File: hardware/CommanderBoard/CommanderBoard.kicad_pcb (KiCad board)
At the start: 2 copper layers, 63.5 x 106.7 mm, 42 parts, among them J1 Conn_01x22, J1BUS1 Conn_02x04_Odd_Even, J1BUS2 Conn_02x04_Odd_Even, J2 Conn_01x22, J2BUS1 Conn_01x02, J2BUS2 Conn_01x02, J3 HUB75, J4 Conn_01x22, SW1 SW_SPDT, SW2 SW_DP3T, SW3 SW_DP3T, SW4 SW_DP3T

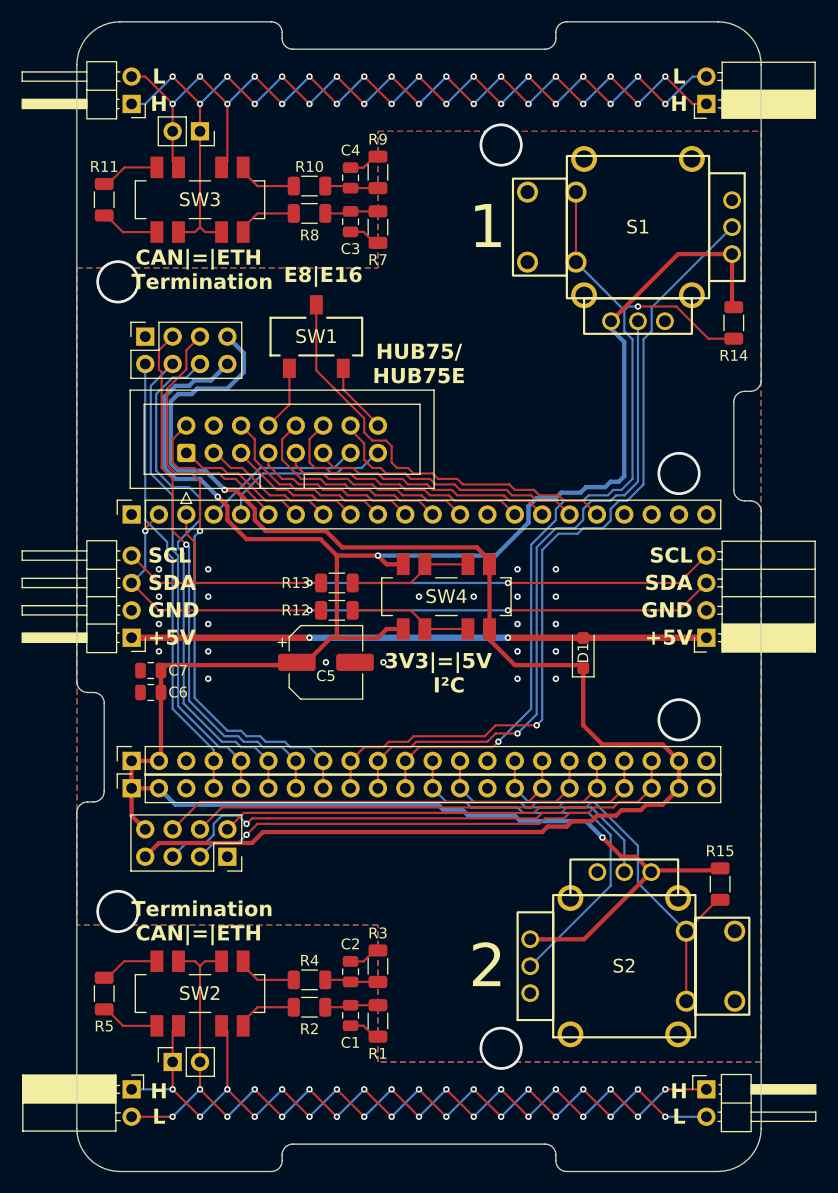
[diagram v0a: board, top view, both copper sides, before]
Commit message: Minor imrpovements in positions and footprints.
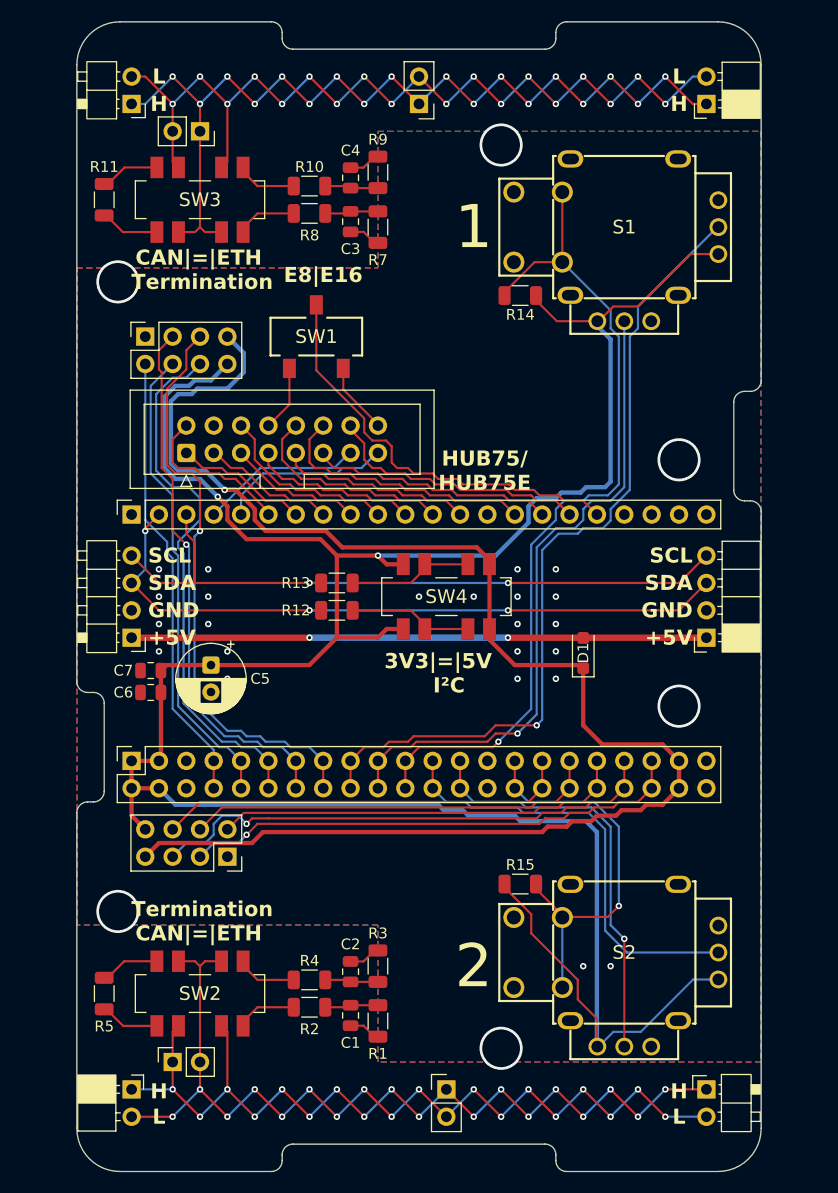
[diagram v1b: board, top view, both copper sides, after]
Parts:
- removed J4: Conn_01x22, Connector_PinSocket_2.54mm:PinSocket_1x22_P2.54mm_Vertical
- added BUS_TAP1: Conn_01x02_Socket, Connector_PinHeader_2.54mm:PinHeader_1x02_P2.54mm_Vertical, F.Cu at (129.5, 121.9)
- added BUS_TAP2: Conn_01x02_Socket, Connector_PinHeader_2.54mm:PinHeader_1x02_P2.54mm_Vertical, F.Cu at (127.0, 30.5)
- C5: footprint Capacitor_SMD:CP_Elec_6.3x7.7 -> Capacitor_THT:CP_Radial_D6.3mm_P2.50mm
- J2: value Conn_01x22 -> Conn_02x22; footprint Connector_PinSocket_2.54mm:PinSocket_1x22_P2.54mm_Vertical -> Connector_PinSocket_2.54mm:PinSocket_2x22_P2.54mm_Vertical
- moved R14 20.0 mm to (136.4, 48.3), turned to 180 degrees
- moved R15 18.5 mm to (136.4, 102.9), turned to 0 degrees
- moved C5 10.7 mm to (107.7, 82.5), turned to -90 degrees
- moved S2 1.27 mm to (146.1, 109.2), turned to -90 degrees
- moved S1 1.27 mm to (146.1, 41.9)
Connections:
- J2 pad 10: S1hCh -> SCLK2
- J2 pad 11: BTN1 -> CS_N2
- J2 pad 12: S2vCh -> CS_N2
- J2 pad 13: S2hCh -> RxD2/MOSI2
- J2 pad 14: unconnected-(J2-Pin_14-Pad14) -> RxD2/MOSI2
- J2 pad 15: BTN2 -> TxD2/MISO2
- J2 pad 16: CS_N1 -> TxD2/MISO2
- J2 pad 17: SCLK1 -> S1vCh
- J2 pad 18: IRQ_N1 -> S1vCh
- J2 pad 19: TxD1/MISO1 -> S1hCh
- J2 pad 20: RxD1/MOSI1 -> S1hCh
- J2 pad 21: +5V -> BTN1
- J2 pad 22: GNDREF -> BTN1
- J2 pad 3: unconnected-(J2-Pin_3-Pad3) -> +3V3
- J2 pad 4: IRQ_N2 -> +3V3
- J2 pad 5: SCLK2 -> unconnected-(J2-Pin_5-Pad5)
- J2 pad 6: CS_N2 -> unconnected-(J2-Pin_6-Pad6)
- J2 pad 7: RxD2/MOSI2 -> IRQ_N2
- J2 pad 8: TxD2/MISO2 -> IRQ_N2
- J2 pad 9: S1vCh -> SCLK2
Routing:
- net +3V3: track 222.3 -> 248.6 mm, vias 3 -> 2
- net S2hCh: track 22.7 -> 38.9 mm, vias 0 -> 1
- net BTN1: track 84.3 -> 78.6 mm, vias 2 -> 1
- net S2vCh: track 36.1 -> 40.9 mm
- net S1hCh: track 62.0 -> 61.0 mm
- net S1vCh: track 77.5 -> 76.6 mm
- net BTN2: track 36.8 -> 37.3 mm, vias 0 -> 1
- net BUS2L: vias 19 -> 18
- net BUS2H: vias 19 -> 18
- net BUS1L: vias 19 -> 18
- net BUS1H: vias 19 -> 18

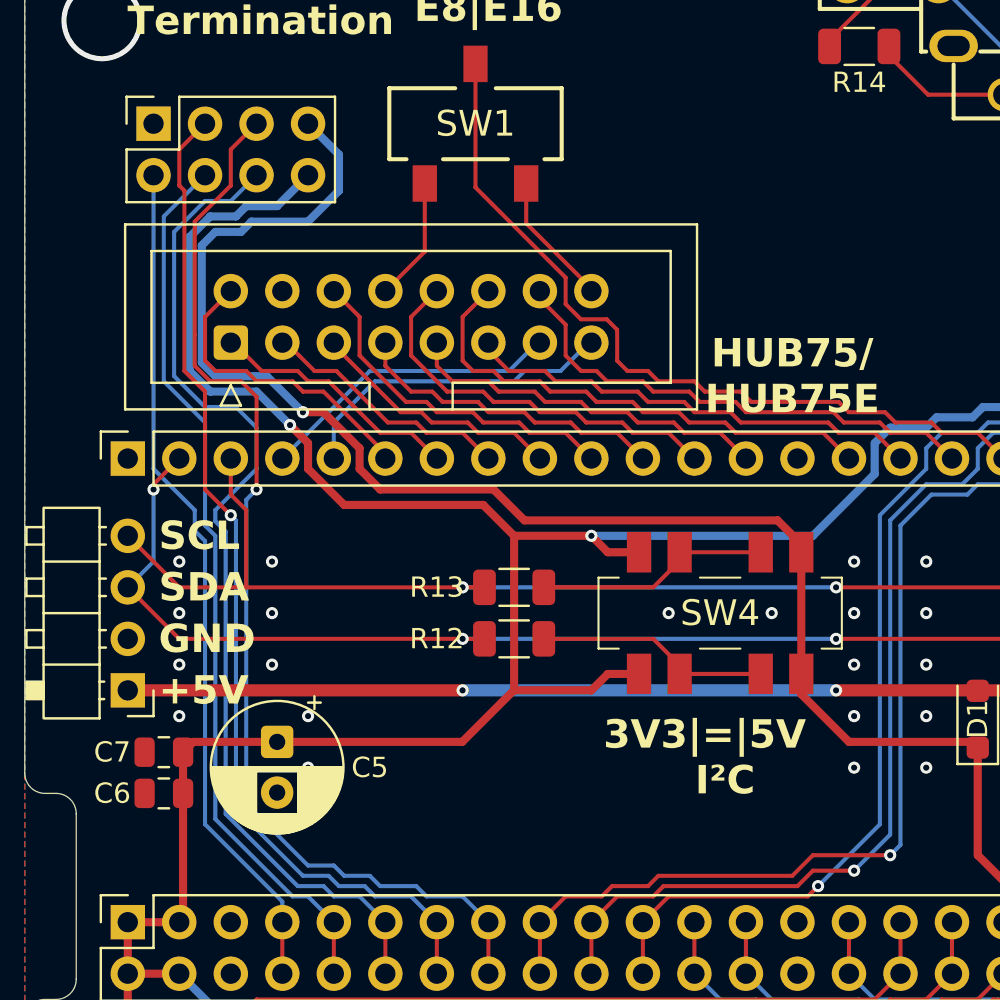
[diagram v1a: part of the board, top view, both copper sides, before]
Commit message: Removed ThumbstickTest. Minor pcb cosmetics.
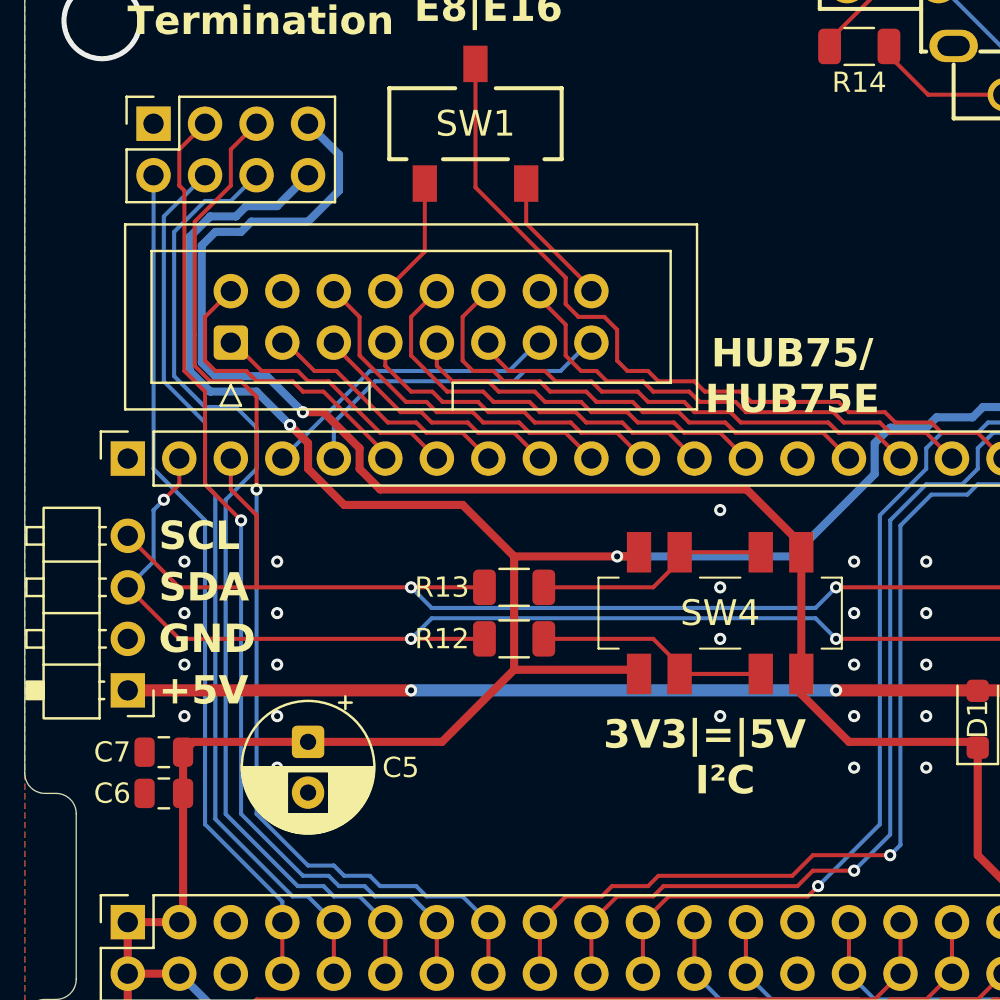
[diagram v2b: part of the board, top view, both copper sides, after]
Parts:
- moved C5 1.52 mm to (109.2, 82.5)
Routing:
- net I2C_SCL: track 63.2 -> 66.8 mm
- net I2C_SDA: track 63.9 -> 67.3 mm
- net +3V3: track 248.6 -> 246.1 mm
- net GNDREF: vias 29 -> 31

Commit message: PCB cosmetics.
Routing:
- net H75_G1: track 15.0 -> 12.3 mm, vias 0 -> 1
- net TxD2/MISO2: track 53.6 -> 56.1 mm
- net RxD2/MOSI2: track 50.2 -> 51.3 mm
- net H75_OE: track 16.1 -> 15.1 mm
- net H75_CLK: track 15.1 -> 16.0 mm
- net +3V3: track 246.1 -> 246.7 mm
- net +5V: track 138.9 -> 138.7 mm, vias 1 -> 0
- net H75_B1: vias 0 -> 1
- net GNDREF: vias 31 -> 32
